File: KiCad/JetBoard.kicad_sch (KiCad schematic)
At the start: 3 parts, among them U6 TYPE-C 16P LCH10.5-A 143

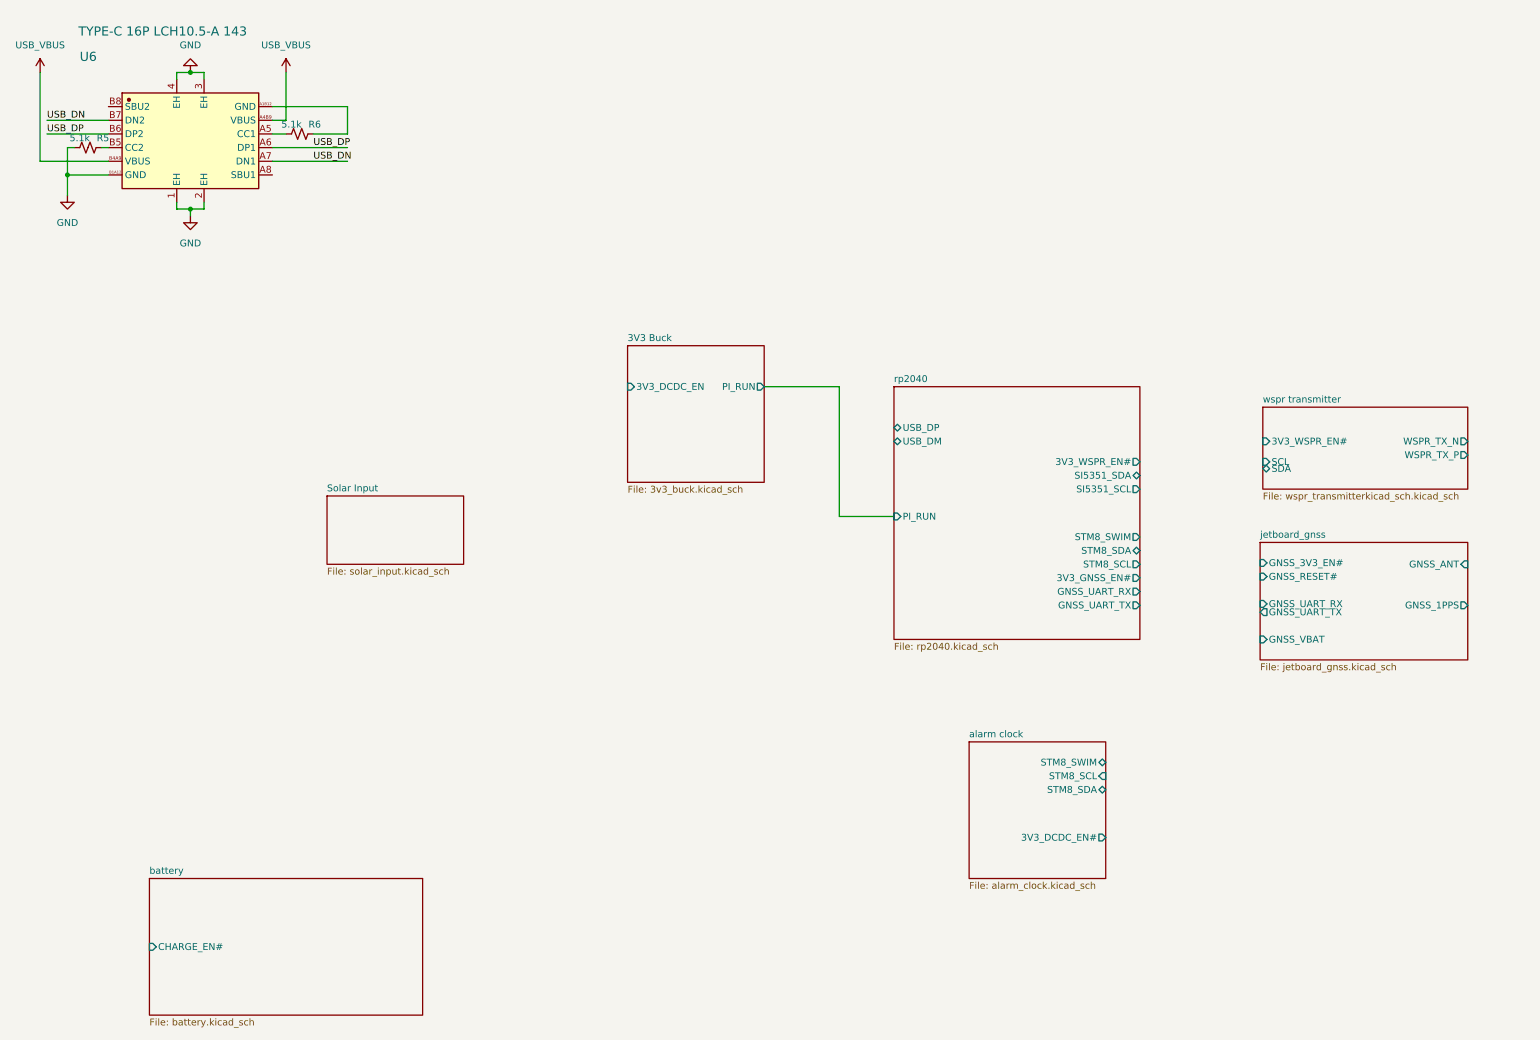
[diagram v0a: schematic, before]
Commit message: Start of docs and design incremental progress
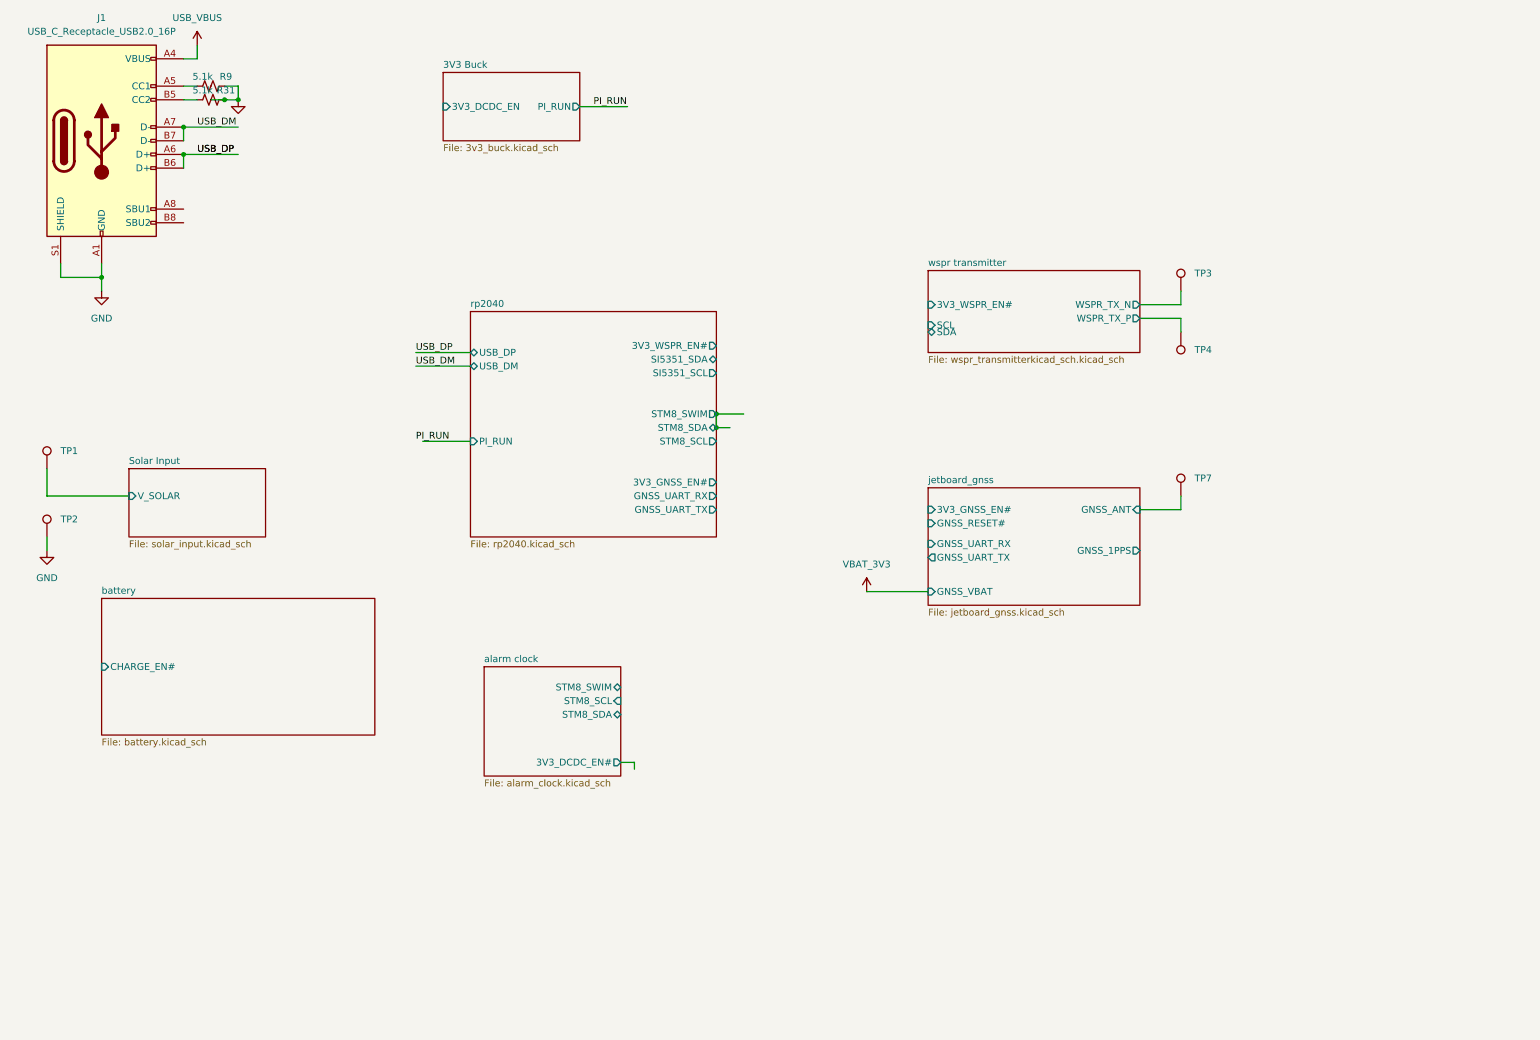
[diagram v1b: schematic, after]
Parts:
- removed R5, R6: 5.1k, Resistor_SMD:R_0402_1005Metric, symbol Device:R_Small_US
- removed U6: TYPE-C 16P LCH10.5-A 143, symbol TYPE-C 16P LCH10.5-A 143
- added J1: USB_C_Receptacle_USB2.0_16P, Connector_USB:USB_C_Receptacle_GCT_USB4105-xx-A_16P_TopMnt_Horizontal, symbol Connector:USB_C_Receptacle_USB2.0_16P
- added R31, R9: 5.1k, Resistor_SMD:R_0402_1005Metric, symbol Device:R_Small_US
- added TP1, TP2, TP3, TP4, TP7: TestPoint, TestPoint:TestPoint_Pad_2.5x2.5mm, symbol Connector:TestPoint
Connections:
- net GND: now also J1.A1 (GND), J1.A12 (GND), J1.B1 (GND), J1.B12 (GND), J1.S1 (SHIELD), R31.2, R9.2, TP2.1
- net USB_DP: now also J1.A6 (D+), J1.B6 (D+)
- net USB_VBUS: now also J1.A4 (VBUS), J1.A9 (VBUS), J1.B4 (VBUS), J1.B9 (VBUS)
- net jetboard_gnss/GNSS_ANT: now also TP7.1
- net wspr transmitter/WSPR_TX_N: now also TP3.1
- net wspr transmitter/WSPR_TX_P: now also TP4.1
- new net: J1.A5 (CC1), R9.1
- new net: J1.B5 (CC2), R31.1
- new net Solar Input/V_SOLAR: TP1.1
- new net USB_DM: J1.A7 (D-), J1.B7 (D-)
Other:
- sheet Solar Input ports: added V_SOLAR; removed none
- sheet jetboard_gnss ports: added 3V3_GNSS_EN#; removed GNSS_3V3_EN#

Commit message: Update schematic and board
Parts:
- added H1, H2: MountingHole, MountingHole:ToolingHole_1.152mm, symbol Mechanical:MountingHole
- TP3, TP4: footprint TestPoint:TestPoint_Pad_2.5x2.5mm -> TestPoint:TestPoint_Pad_1.5x1.5mm
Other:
- sheet jetboard_gnss renamed gnss

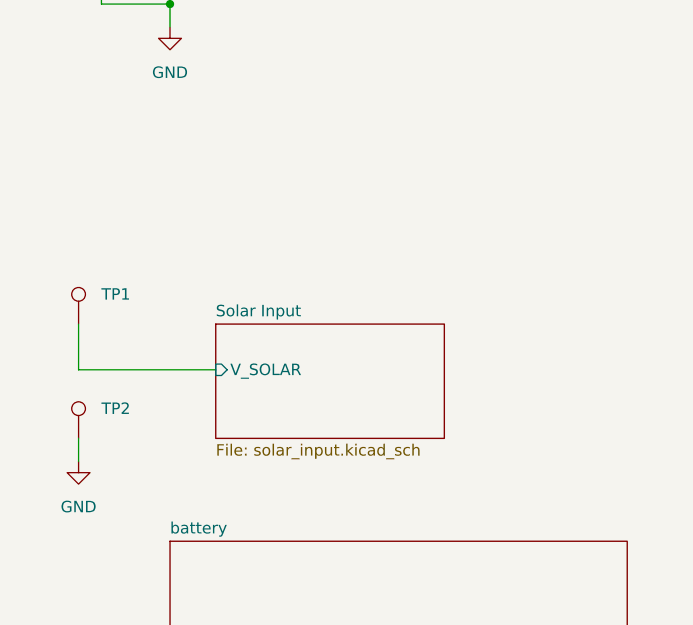
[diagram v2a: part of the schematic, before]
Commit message: Schematic and PCB updates
- Add basic solar modules and 3d step
- shrink PCB size
- need to find USB connector that doesn't go through the board
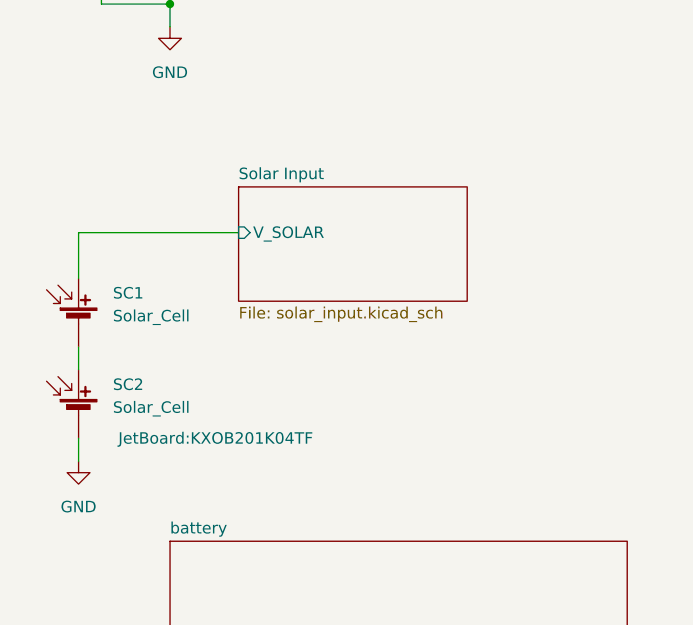
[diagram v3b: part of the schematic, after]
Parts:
- removed TP1, TP2: TestPoint, TestPoint:TestPoint_Pad_2.5x2.5mm, symbol Connector:TestPoint
- added SC1, SC2: Solar_Cell, JetBoard:KXOB201K04TF, symbol Device:Solar_Cell
- J1: footprint Connector_USB:USB_C_Receptacle_GCT_USB4105-xx-A_16P_TopMnt_Horizontal -> Connector_USB:USB_C_Receptacle_G-Switch_GT-USB-7051x
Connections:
- net GND: now also SC2.2 (-)
- net Solar Input/V_SOLAR: now also SC1.1 (+)
- new net: SC1.2 (-), SC2.1 (+)

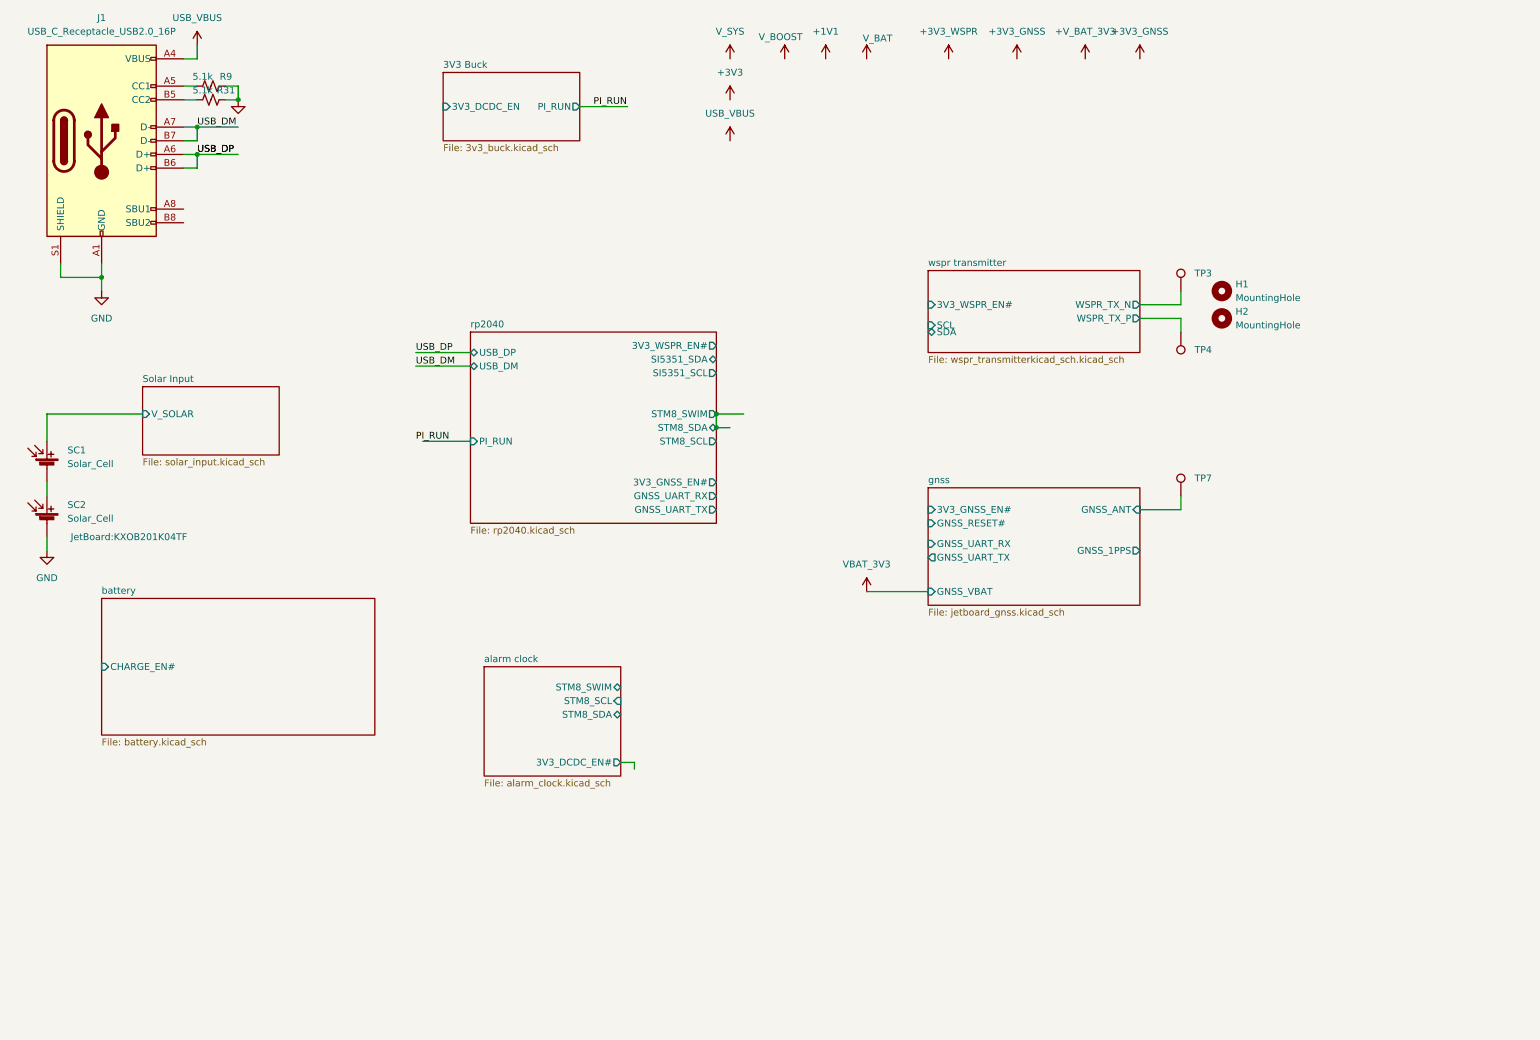
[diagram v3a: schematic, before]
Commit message: 3D model fixes and change to 3.0V buck
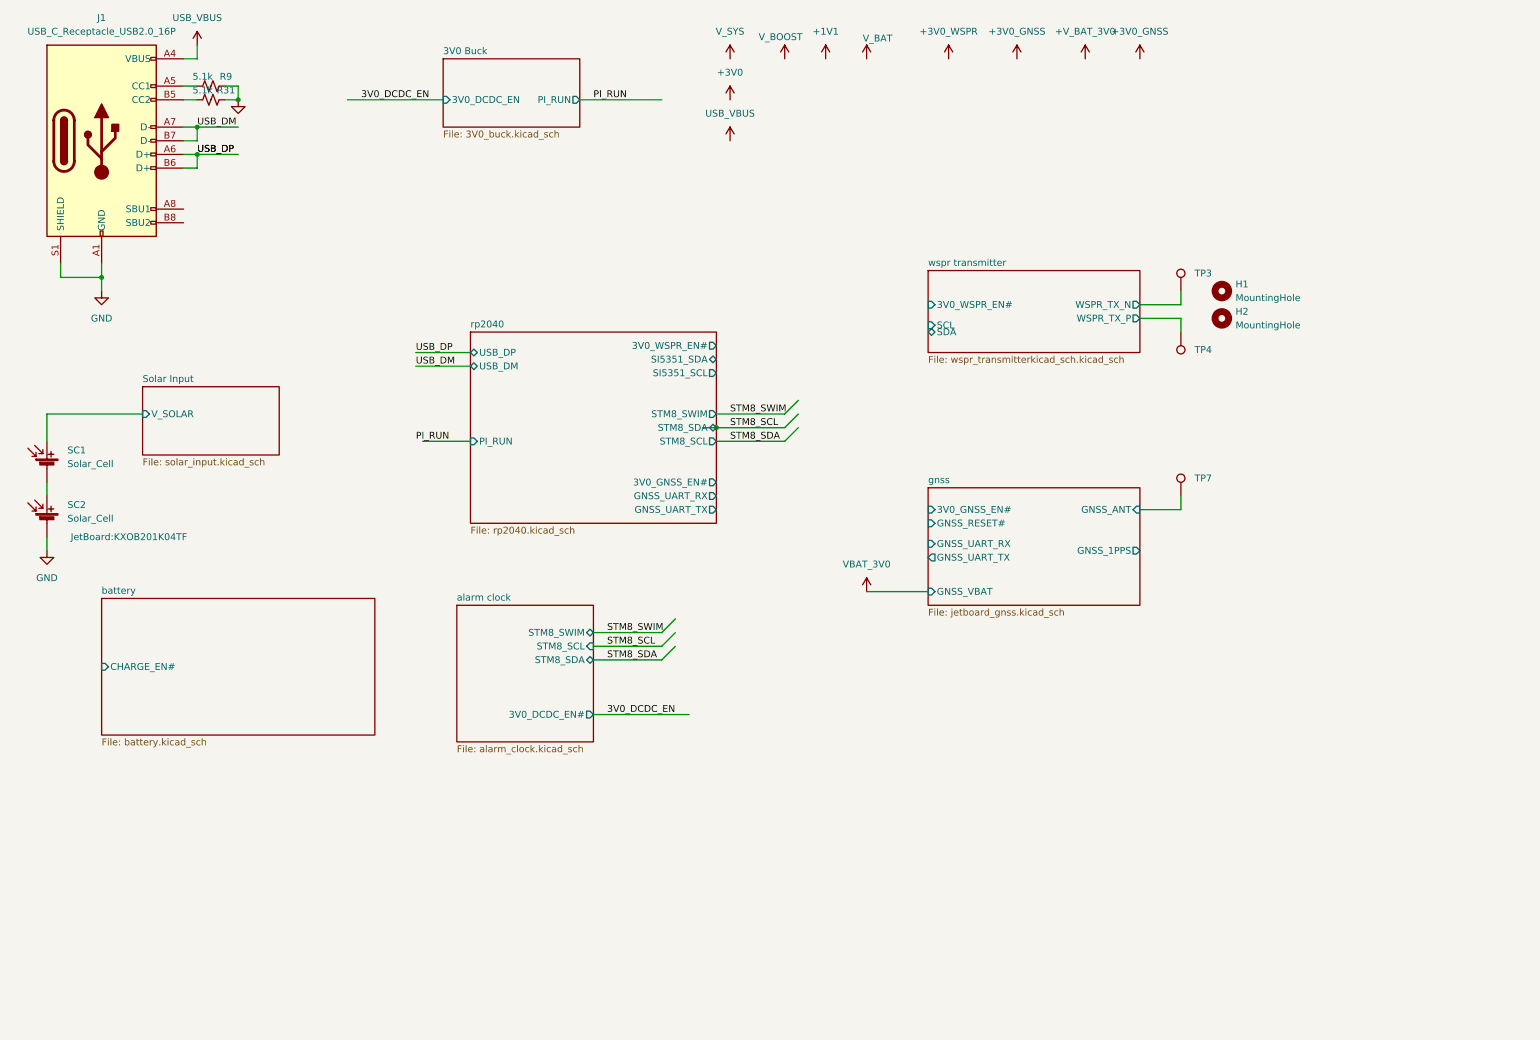
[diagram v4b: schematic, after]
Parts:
- J1: footprint Connector_USB:USB_C_Receptacle_G-Switch_GT-USB-7051x -> Connector_USB:USB_C_Receptacle_GCT_USB4110
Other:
- sheet 3V3 Buck renamed 3V0 Buck
- sheet 3V0 Buck: file 3v3_buck.kicad_sch -> 3V0_buck.kicad_sch
- sheet 3V0 Buck ports: added 3V0_DCDC_EN; removed 3V3_DCDC_EN
- sheet alarm clock ports: added 3V0_DCDC_EN#; removed 3V3_DCDC_EN#
- sheet gnss ports: added 3V0_GNSS_EN#; removed 3V3_GNSS_EN#
- sheet rp2040 ports: added 3V0_GNSS_EN#, 3V0_WSPR_EN#; removed 3V3_GNSS_EN#, 3V3_WSPR_EN#
- sheet wspr transmitter ports: added 3V0_WSPR_EN#; removed 3V3_WSPR_EN#

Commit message: Schematic changes
- Changed to STM8L050
- Changed to SPI interface for STM8 bootloader
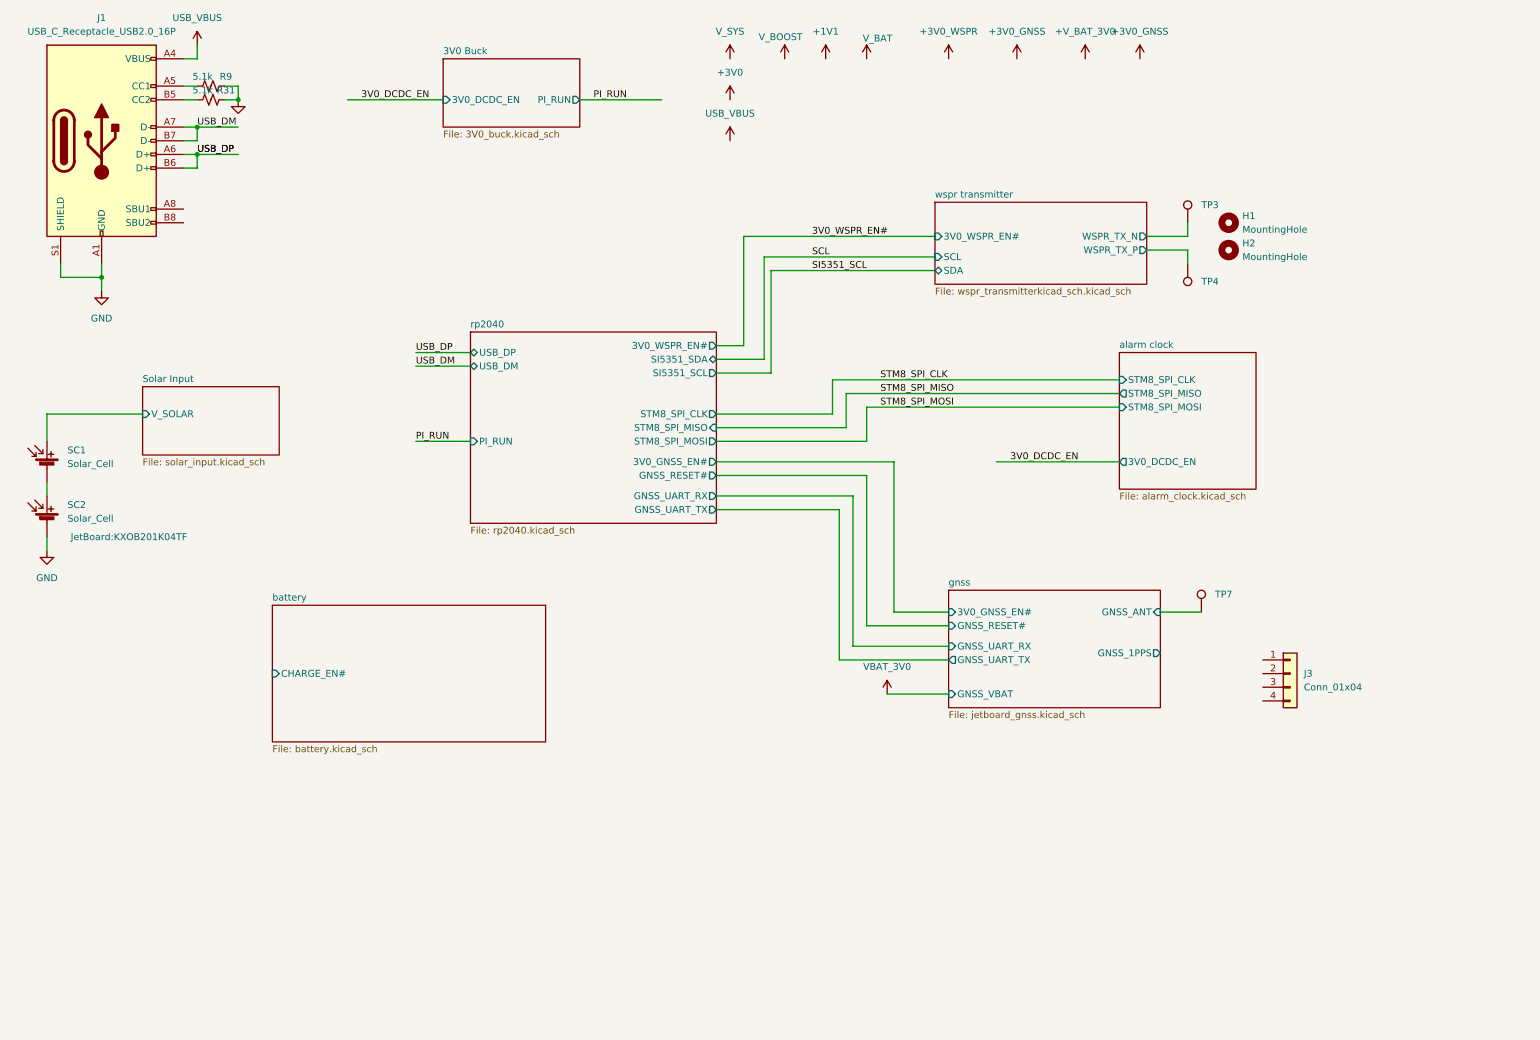
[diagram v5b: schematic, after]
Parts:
- added J3: Conn_01x04, Connector_JST:JST_SH_SM04B-SRSS-TB_1x04-1MP_P1.00mm_Horizontal, symbol Connector_Generic:Conn_01x04
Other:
- sheet alarm clock ports: added 3V0_DCDC_EN, STM8_SPI_CLK, STM8_SPI_MISO, STM8_SPI_MOSI; removed 3V0_DCDC_EN#, STM8_SCL, STM8_SDA, STM8_SWIM
- sheet rp2040 ports: added GNSS_RESET#, STM8_SPI_CLK, STM8_SPI_MISO, STM8_SPI_MOSI; removed STM8_SCL, STM8_SDA, STM8_SWIM
- moved on the sheet: H1, H2, TP3, TP4, TP7
